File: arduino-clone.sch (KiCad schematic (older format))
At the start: 13 parts, among them U1 24LC1025, U2 24LC1025, U3 DS13375+, U4 ATMEGA328P-AU, Y1 Crystal 32MHz, Y2 Crystal 16MHz

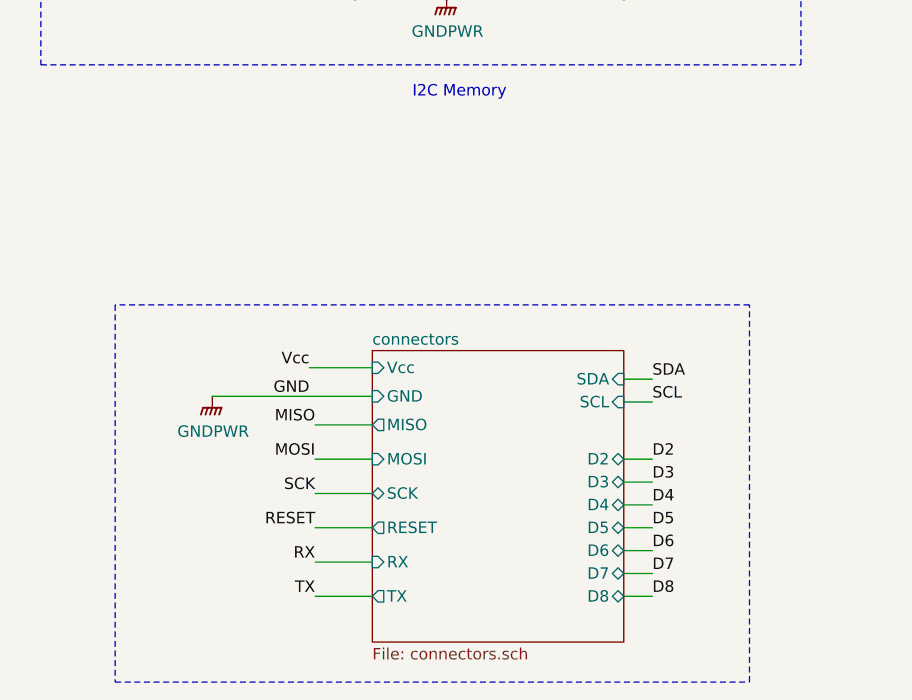
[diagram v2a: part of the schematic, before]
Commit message: [pcbnew] add 2 and 4 layer autorouted pcbs
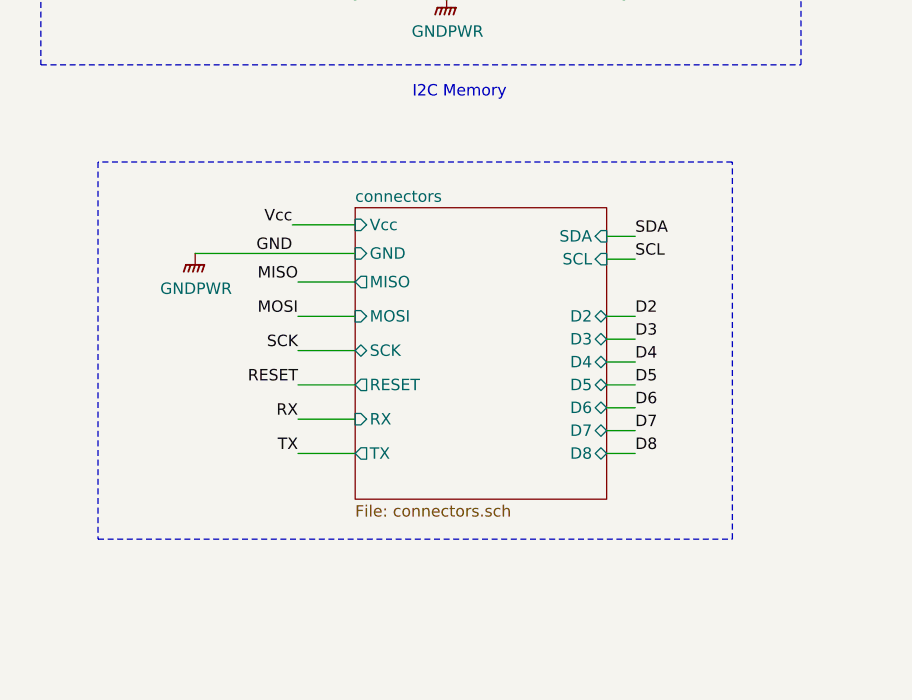
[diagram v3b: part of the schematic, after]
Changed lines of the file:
@@
 $EndComp
 $Sheet
-S 3900 5675 1100 1275
+S 3825 5050 1100 1275
 U 5EE59D89
 F0 "connectors" 50
 F1 "connectors.sch" 50
-F2 "MISO" O L 3900 6000 50
-F3 "SCK" B L 3900 6300 50
-F4 "Vcc" I L 3900 5750 50
-F5 "MOSI" I L 3900 6150 50
-F6 "RESET" O L 3900 6450 50
-F7 "GND" I L 3900 5875 50
-F8 "RX" I L 3900 6600 50
-F9 "TX" O L 3900 6750 50
-F10 "SDA" I R 5000 5800 50
-F11 "SCL" I R 5000 5900 50
-F12 "D2" B R 5000 6150 50
-F13 "D3" B R 5000 6250 50
-F14 "D4" B R 5000 6350 50
-F15 "D5" B R 5000 6450 50
-F16 "D6" B R 5000 6550 50
-F17 "D7" B R 5000 6650 50
-F18 "D8" B R 5000 6750 50
+F2 "MISO" O L 3825 5375 50
+F3 "SCK" B L 3825 5675 50
+F4 "Vcc" I L 3825 5125 50
+F5 "MOSI" I L 3825 5525 50
+F6 "RESET" O L 3825 5825 50
+F7 "GND" I L 3825 5250 50
+F8 "RX" I L 3825 5975 50
+F9 "TX" O L 3825 6125 50
+F10 "SDA" I R 4925 5175 50
+F11 "SCL" I R 4925 5275 50
+F12 "D2" B R 4925 5525 50
+F13 "D3" B R 4925 5625 50
+F14 "D4" B R 4925 5725 50
+F15 "D5" B R 4925 5825 50
+F16 "D6" B R 4925 5925 50
+F17 "D7" B R 4925 6025 50
+F18 "D8" B R 4925 6125 50
 $EndSheet
 $Comp
@@
 	1    0    0    -1
 $EndComp
-Text Label 3650 6000 2    50   ~ 0
+Text Label 3575 5375 2    50   ~ 0
 MISO
-Text Label 3650 6150 2    50   ~ 0
+Text Label 3575 5525 2    50   ~ 0
 MOSI
-Text Label 3650 6300 2    50   ~ 0
+Text Label 3575 5675 2    50   ~ 0
 SCK
-Text Label 3650 6450 2    50   ~ 0
+Text Label 3575 5825 2    50   ~ 0
 RESET
 Wire Wire Line
-	3650 6450 3900 6450
-Wire Wire Line
-	3650 6300 3900 6300
-Wire Wire Line
-	3900 6150 3650 6150
-Wire Wire Line
-	3650 6000 3900 6000
-Text Label 3625 5750 2    50   ~ 0
-Vcc
-Wire Wire Line
-	3625 5750 3900 5750
-Text Label 3625 5875 2    50   ~ 0
+	3575 5825 3825 5825
+Wire Wire Line
+	3575 5675 3825 5675
+Wire Wire Line
+	3825 5525 3575 5525
+Wire Wire Line
+	3575 5375 3825 5375
+Text Label 3550 5125 2    50   ~ 0
+Vcc
+Wire Wire Line
+	3550 5125 3825 5125
+Text Label 3550 5250 2    50   ~ 0
 GND
 Text Label 8075 2225 2    50   ~ 0
@@
 L power:GNDPWR #PWR0101
 U 1 1 5EE978D3
-P 3200 5875
-F 0 "#PWR0101" H 3200 5675 50  0001 C CNN
-F 1 "GNDPWR" H 3204 5721 50  0000 C CNN
-F 2 "" H 3200 5825 50  0001 C CNN
-F 3 "" H 3200 5825 50  0001 C CNN
-	1    3200 5875
-	1    0    0    -1
-$EndComp
-Wire Wire Line
-	3200 5875 3900 5875
-Text Label 5125 6150 0    50   ~ 0
+P 3125 5250
+F 0 "#PWR0101" H 3125 5050 50  0001 C CNN
+F 1 "GNDPWR" H 3129 5096 50  0000 C CNN
+F 2 "" H 3125 5200 50  0001 C CNN
+F 3 "" H 3125 5200 50  0001 C CNN
+	1    3125 5250
+	1    0    0    -1
+$EndComp
+Wire Wire Line
+	3125 5250 3825 5250
+Text Label 5050 5525 0    50   ~ 0
 D2
-Text Label 5125 6250 0    50   ~ 0
+Text Label 5050 5625 0    50   ~ 0
 D3
-Text Label 5125 6350 0    50   ~ 0
+Text Label 5050 5725 0    50   ~ 0
 D4
-Text Label 5125 6450 0    50   ~ 0
+Text Label 5050 5825 0    50   ~ 0
 D5
-Text Label 5125 6550 0    50   ~ 0
+Text Label 5050 5925 0    50   ~ 0
 D6
-Text Label 5125 6650 0    50   ~ 0
+Text Label 5050 6025 0    50   ~ 0
 D7
-Text Label 5125 6750 0    50   ~ 0
+Text Label 5050 6125 0    50   ~ 0
 D8
 Wire Wire Line
-	5000 6750 5125 6750
-Wire Wire Line
-	5125 6650 5000 6650
-Wire Wire Line
-	5125 6550 5000 6550
-Wire Wire Line
-	5125 6450 5000 6450
-Wire Wire Line
-	5125 6350 5000 6350
-Wire Wire Line
-	5125 6250 5000 6250
-Wire Wire Line
-	5125 6150 5000 6150
-Text Label 5125 5800 0    50   ~ 0
+	4925 6125 5050 6125
+Wire Wire Line
+	5050 6025 4925 6025
+Wire Wire Line
+	5050 5925 4925 5925
+Wire Wire Line
+	5050 5825 4925 5825
+Wire Wire Line
+	5050 5725 4925 5725
+Wire Wire Line
+	5050 5625 4925 5625
+Wire Wire Line
+	5050 5525 4925 5525
+Text Label 5050 5175 0    50   ~ 0
 SDA
-Text Label 5125 5900 0    50   ~ 0
+Text Label 5050 5275 0    50   ~ 0
 SCL
 Wire Wire Line
-	5125 5900 5000 5900
-Wire Wire Line
-	5125 5800 5000 5800
-Text Label 3650 6600 2    50   ~ 0
+	5050 5275 4925 5275
+Wire Wire Line
+	5050 5175 4925 5175
+Text Label 3575 5975 2    50   ~ 0
 RX
-Text Label 3650 6750 2    50   ~ 0
+Text Label 3575 6125 2    50   ~ 0
 TX
 Wire Wire Line
-	3650 6750 3900 6750
-Wire Wire Line
-	3650 6600 3900 6600
+	3575 6125 3825 6125
+Wire Wire Line
+	3575 5975 3825 5975
 Text Label 8075 1225 2    50   ~ 0
 D3
@@
 	2450 3100 2450 4425
 Wire Notes Line
-	2775 5475 2775 7125
-Wire Notes Line
-	2775 7125 5550 7125
-Wire Notes Line
-	5550 7125 5550 5475
-Wire Notes Line
-	5550 5475 2775 5475
+	2700 4850 2700 6500
+Wire Notes Line
+	2700 6500 5475 6500
+Wire Notes Line
+	5475 6500 5475 4850
+Wire Notes Line
+	5475 4850 2700 4850
 Wire Notes Line
 	6600 4425 6600 625
